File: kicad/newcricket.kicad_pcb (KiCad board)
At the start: 2 copper layers, 32.5 x 49 mm, 25 parts, among them IC1 ATTINY85-P, Q1 Q_NPN_BCE, SW1 SW_PUSH, SW2 SW_PUSH, SW3 SWITCH_INV, U1 LM335

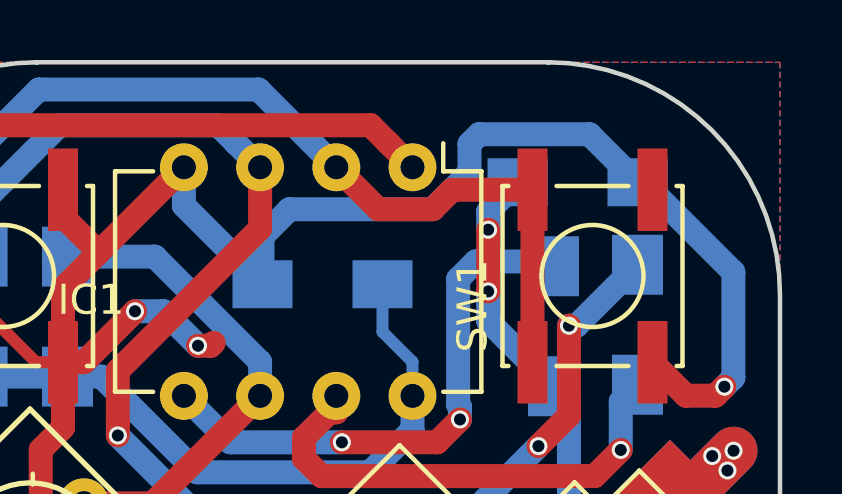
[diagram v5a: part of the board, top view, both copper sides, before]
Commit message: Fixed the clearances on a filled zone near ATtiny.
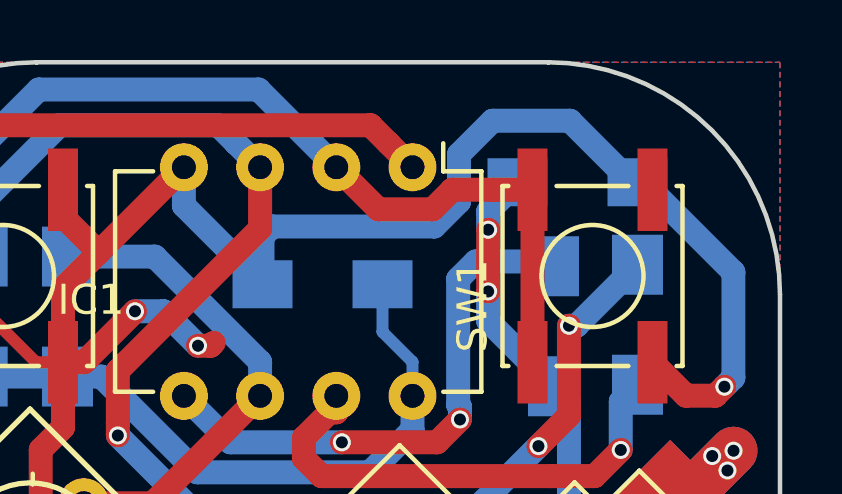
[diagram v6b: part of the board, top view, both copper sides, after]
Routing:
- net GND: track 173.8 -> 174.5 mm
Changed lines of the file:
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@@
     (thickness 1.6)
     (drawings 8)
-    (tracks 249)
+    (tracks 250)
     (zones 0)
     (modules 25)
@@
     (visible_elements FFFFFF7F)
     (pcbplotparams
-      (layerselection 0x00030_80000001)
+      (layerselection 0x010f0_80000001)
       (usegerberextensions false)
       (excludeedgelayer true)
@@
       (outputformat 1)
       (mirror false)
-      (drillshape 1)
+      (drillshape 0)
       (scaleselection 1)
       (outputdirectory ""))
@@
   (segment (start 80.586292 97.161292) (end 79.675 96.25) (width 0.8) (layer F.Cu) (net 2))
   (segment (start 79.675 96.25) (end 78.125 96.25) (width 0.8) (layer F.Cu) (net 2))
+  (segment (start 89.45 71.9) (end 89.45 70.3) (width 0.8) (layer B.Cu) (net 3))
+  (segment (start 89.45 70.3) (end 89.775 69.975) (width 0.8) (layer B.Cu) (net 3))
+  (segment (start 89.775 69.975) (end 95.175 69.975) (width 0.8) (layer B.Cu) (net 3))
+  (segment (start 95.175 69.975) (end 96 69.15) (width 0.8) (layer B.Cu) (net 3))
+  (segment (start 96 69.15) (end 96 67.569998) (width 0.8) (layer B.Cu) (net 3))
+  (segment (start 96 67.569998) (end 97.119998 66.45) (width 0.8) (layer B.Cu) (net 3))
+  (segment (start 97.119998 66.45) (end 99.7 66.45) (width 0.8) (layer B.Cu) (net 3))
+  (segment (start 99.7 66.45) (end 101.75 68.5) (width 0.8) (layer B.Cu) (net 3))
+  (segment (start 101.75 68.5) (end 101.95 68.5) (width 0.8) (layer B.Cu) (net 3))
   (segment (start 82.8 74.5) (end 81.9 74.5) (width 0.4) (layer F.Cu) (net 3))
   (segment (start 81.9 74.5) (end 80.35 72.95) (width 0.4) (layer F.Cu) (net 3))
@@
   (segment (start 81.894439 103.321855) (end 83.882055 103.321855) (width 0.8) (layer B.Cu) (net 3))
   (via (at 104.8462 75.3148) (size 0.6) (drill 0.4) (layers F.Cu B.Cu) (net 3))
-  (segment (start 95.122001 69.400001) (end 96.349999 68.172003) (width 0.8) (layer B.Cu) (net 3))
-  (segment (start 89.45 71.9) (end 89.45 70.3) (width 0.8) (layer B.Cu) (net 3))
-  (segment (start 89.45 70.3) (end 90.349999 69.400001) (width 0.8) (layer B.Cu) (net 3))
-  (segment (start 90.349999 69.400001) (end 95.122001 69.400001) (width 0.8) (layer B.Cu) (net 3))
-  (segment (start 96.349999 68.172003) (end 96.349999 67.219999) (width 0.8) (layer B.Cu) (net 3))
-  (segment (start 96.349999 67.219999) (end 96.669998 66.9) (width 0.8) (layer B.Cu) (net 3))
-  (segment (start 96.669998 66.9) (end 100.35 66.9) (width 0.8) (layer B.Cu) (net 3))
-  (segment (start 100.35 66.9) (end 101.95 68.5) (width 0.8) (layer B.Cu) (net 3))
   (segment (start 86.83 68) (end 86.83 69.28) (width 0.8) (layer B.Cu) (net 3))
   (segment (start 86.83 69.28) (end 89.45 71.9) (width 0.8) (layer B.Cu) (net 3))
